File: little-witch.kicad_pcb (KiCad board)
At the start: 4 copper layers, 65 x 30 mm, 58 parts, among them J1 GCT-USB4105, J2 TMJG0803HENL, J3 Conn_ARM_SWD_TagConnect_TC203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, J4 GCT-USB4105, J5 Conn_02x20_Odd_Even, J6 BOOT0_SEL, SW1 SW_Push, U1 CH32V307RCT6, U2 MXL86110C-AQB-R, Y1 SIT8008BI-73-33N-25.000000

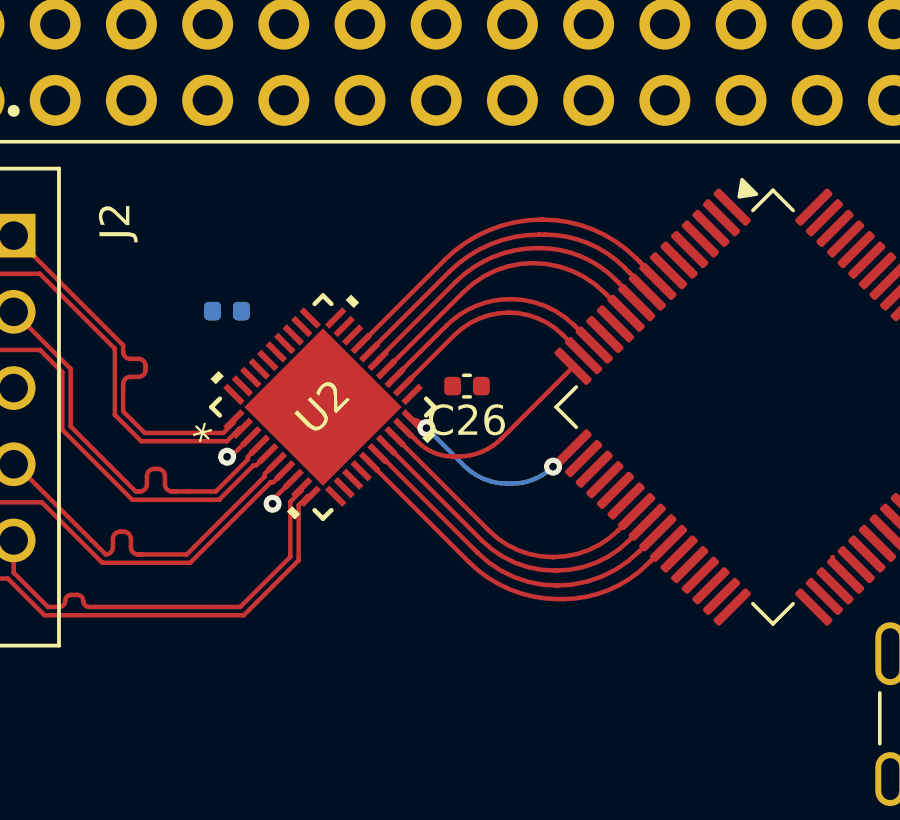
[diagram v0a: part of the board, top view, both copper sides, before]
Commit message: MDI RX/TX length matched
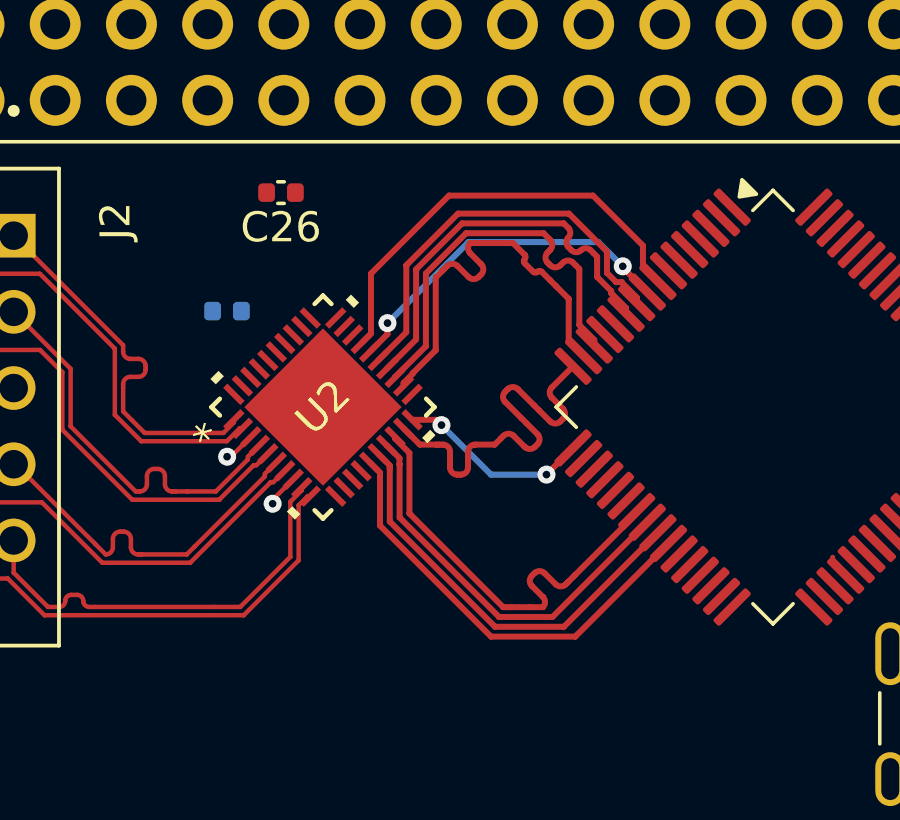
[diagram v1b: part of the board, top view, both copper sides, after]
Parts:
- moved C26 8.95 mm to (128.6, 107.8)
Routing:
- net ETH_TXC: track 7.12 -> 13.6 mm
- net ETH_RXD3: track 7.36 -> 13.6 mm
- net ETH_RXD2: track 8.07 -> 13.5 mm
- net ETH_TXD0: track 10.2 -> 14.5 mm
- net ETH_RXD1: track 9.81 -> 13.6 mm
- net ETH_RXD0: track 10.6 -> 13.7 mm
- net ETH_TXD1: track 10.8 -> 13.5 mm
- net ETH_RXC: track 12.0 -> 14.7 mm
- net ETH_TXD2: track 11.5 -> 14.1 mm
- net ETH_TXD3: track 12.2 -> 14.7 mm
- net ETH_RX_CTL: track 11.3 -> 11.7 mm, vias 0 -> 2

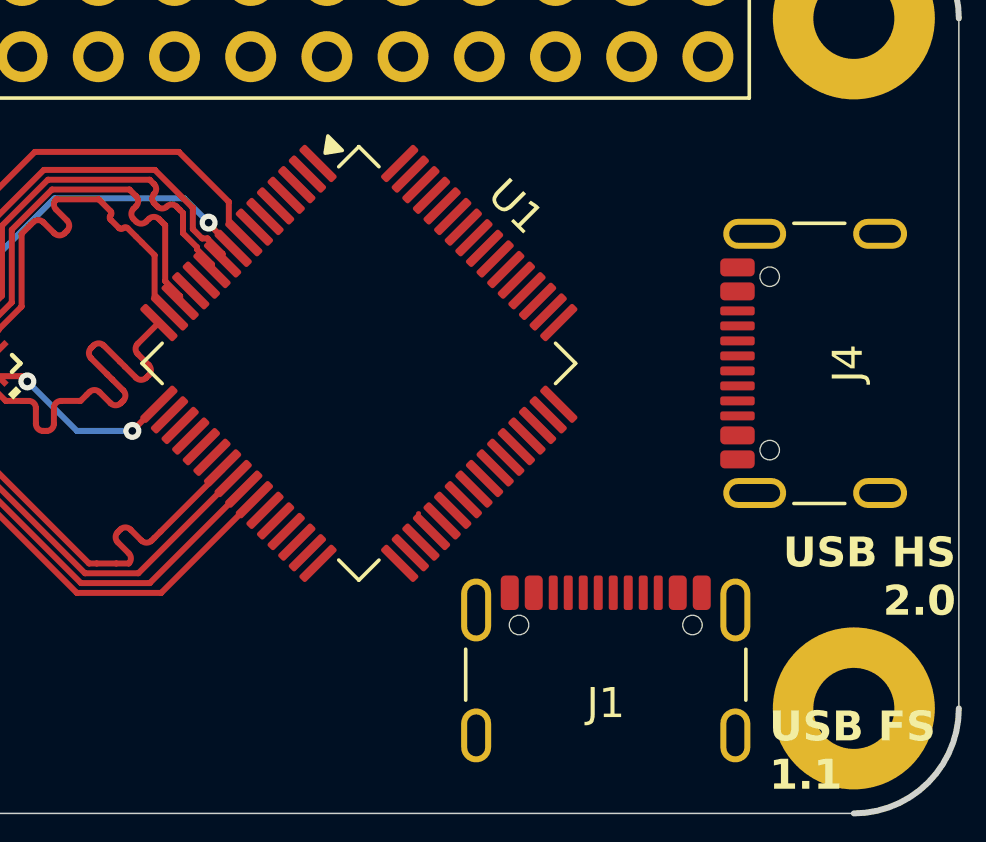
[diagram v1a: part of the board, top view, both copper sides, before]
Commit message: USB routing
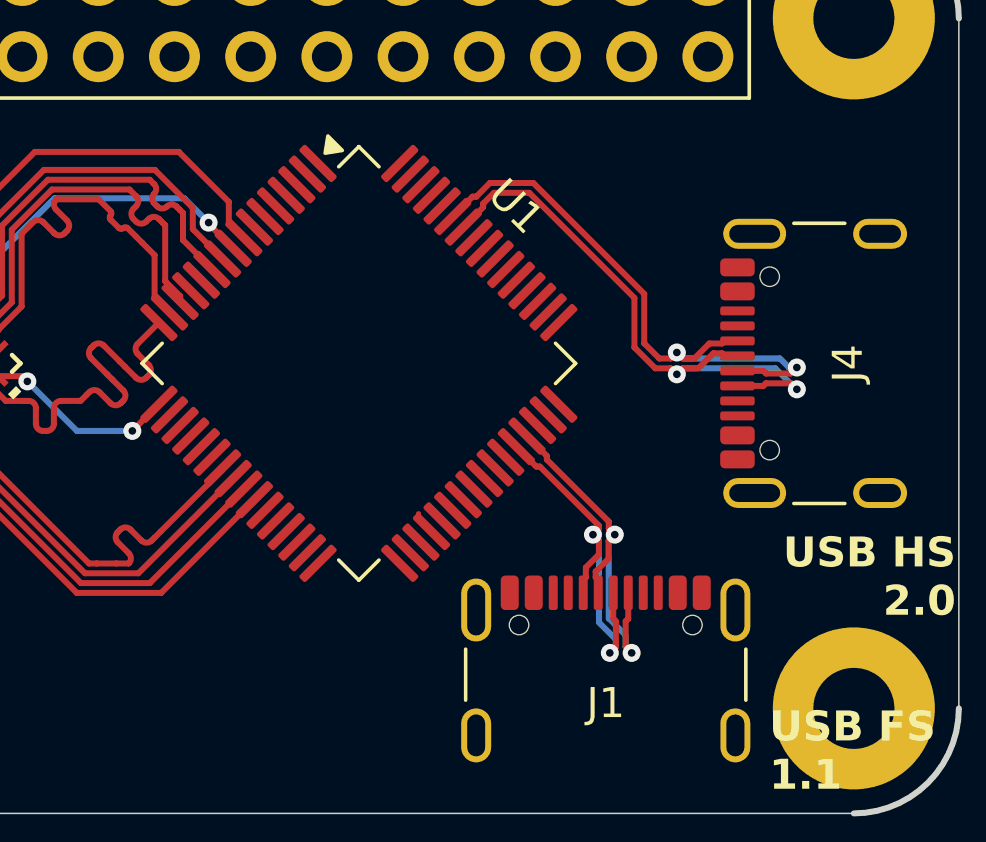
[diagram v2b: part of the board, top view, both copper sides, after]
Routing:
- net USB2_DP: track 0.00 -> 20.1 mm, vias 0 -> 2
- net USB2_DN: track 0.00 -> 20.0 mm, vias 0 -> 2
- net USB1_DP: track 0.00 -> 13.2 mm, vias 0 -> 2
- net USB1_DN: track 0.00 -> 12.9 mm, vias 0 -> 2

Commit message: MCU decoupling
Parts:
- C2, C3, C4, C5, C6: moved to B.Cu
- moved C6 57.3 mm to (152.1, 116.8), turned to 135 degrees
- moved C3 56.6 mm to (139.0, 112.2), turned to -45 degrees
- moved C2 48.9 mm to (143.2, 108.0), turned to -45 degrees
- moved C4 47.1 mm to (138.7, 117.5), turned to 45 degrees
- moved C5 20.6 mm to (143.2, 122.0), turned to 45 degrees
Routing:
- net GND: track 0.00 -> 16.8 mm, vias 0 -> 10
- net +3V3: track 0.00 -> 5.52 mm, vias 0 -> 5

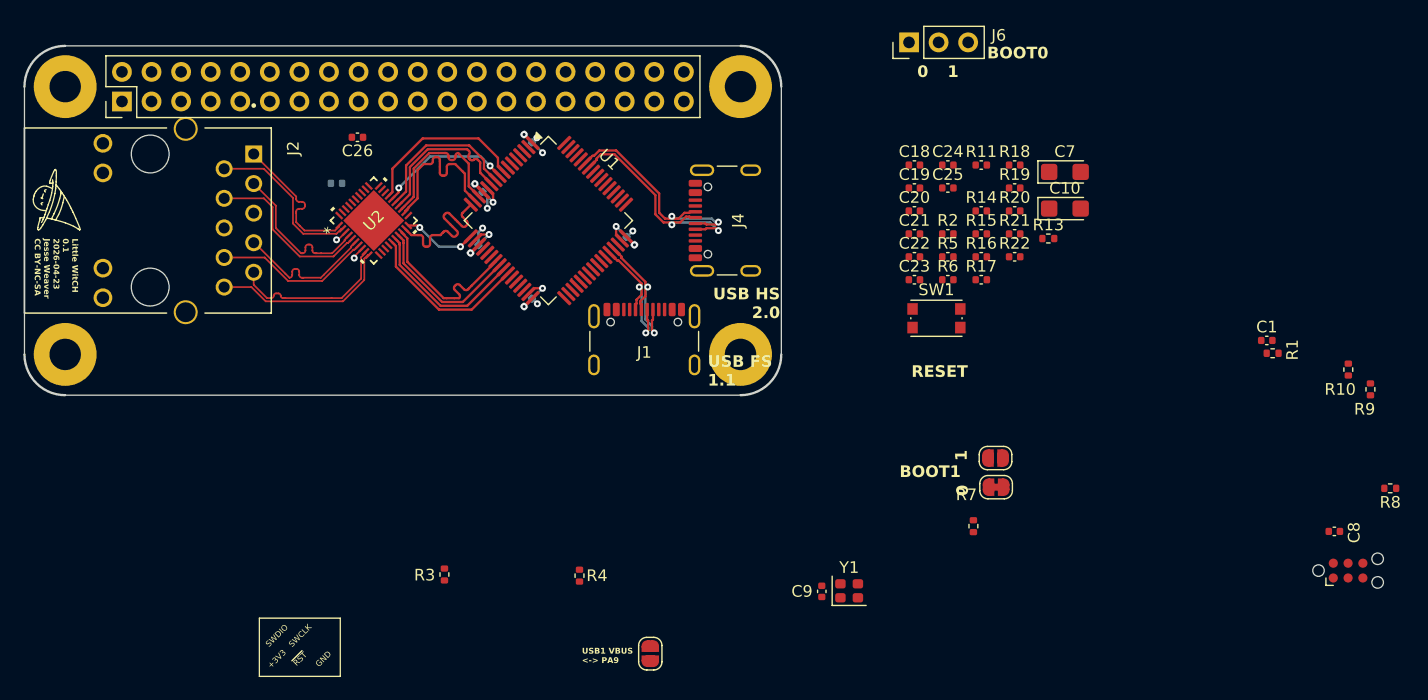
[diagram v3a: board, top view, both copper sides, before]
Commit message: Start on PHY decoupling
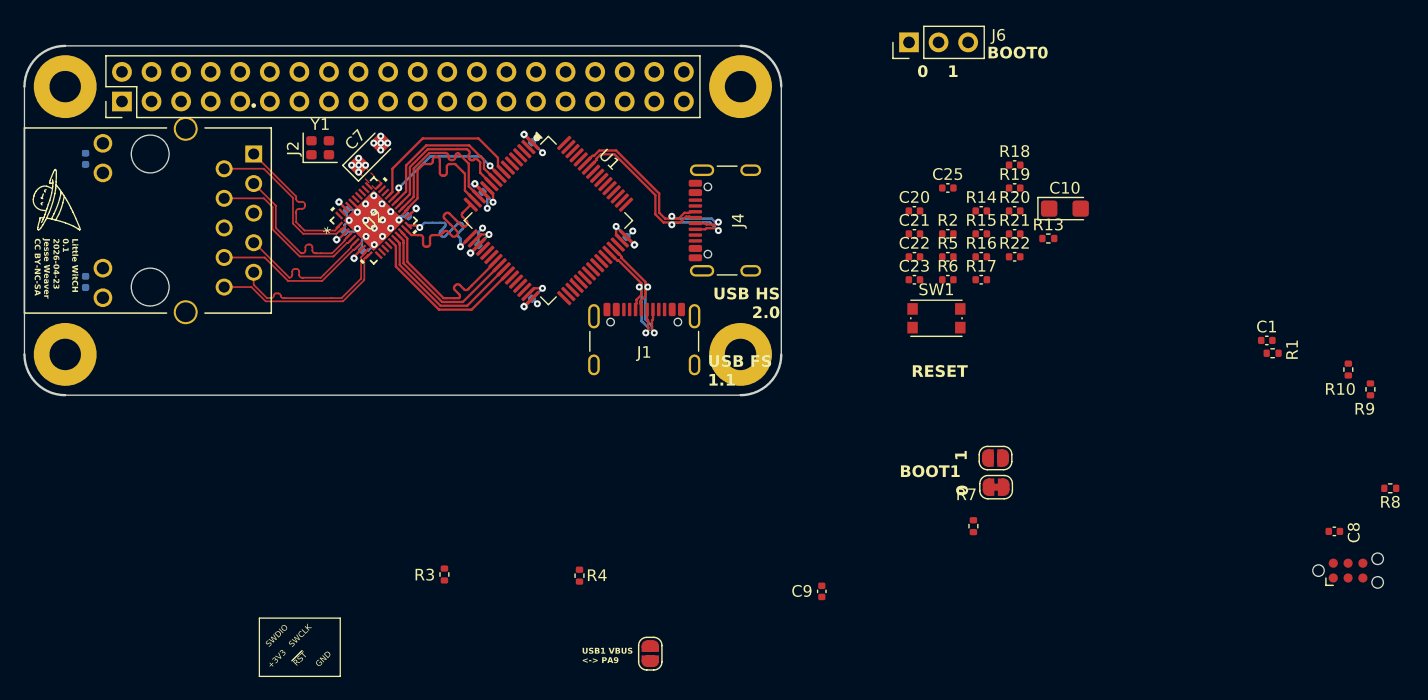
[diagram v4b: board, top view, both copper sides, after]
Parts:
- C18, C19, C24, C26, R11: moved to B.Cu
- moved R11 76.9 mm to (105.2, 109.7), turned to 90 degrees
- moved C7 59.7 mm to (129.7, 109.3), turned to 45 degrees
- moved Y1 59.3 mm to (125.4, 108.8)
- moved C18 49.7 mm to (127.2, 116.3), turned to 45 degrees
- moved C19 48.1 mm to (128.7, 117.9), turned to 45 degrees
- moved C24 46.2 mm to (133.3, 114.3), turned to -135 degrees
- moved R12 23.2 mm to (105.2, 120.3), turned to 90 degrees
- moved C26 6.03 mm to (127.3, 113.8), turned to -45 degrees
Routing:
- net GND: track 16.8 -> 27.3 mm, vias 10 -> 31
- net ETH_TX_CTL: track 6.49 -> 10.6 mm
- net VDD_ETH: track 2.17 -> 3.95 mm, vias 2 -> 9
- added copper zone on F.Cu, net VDD_ETH

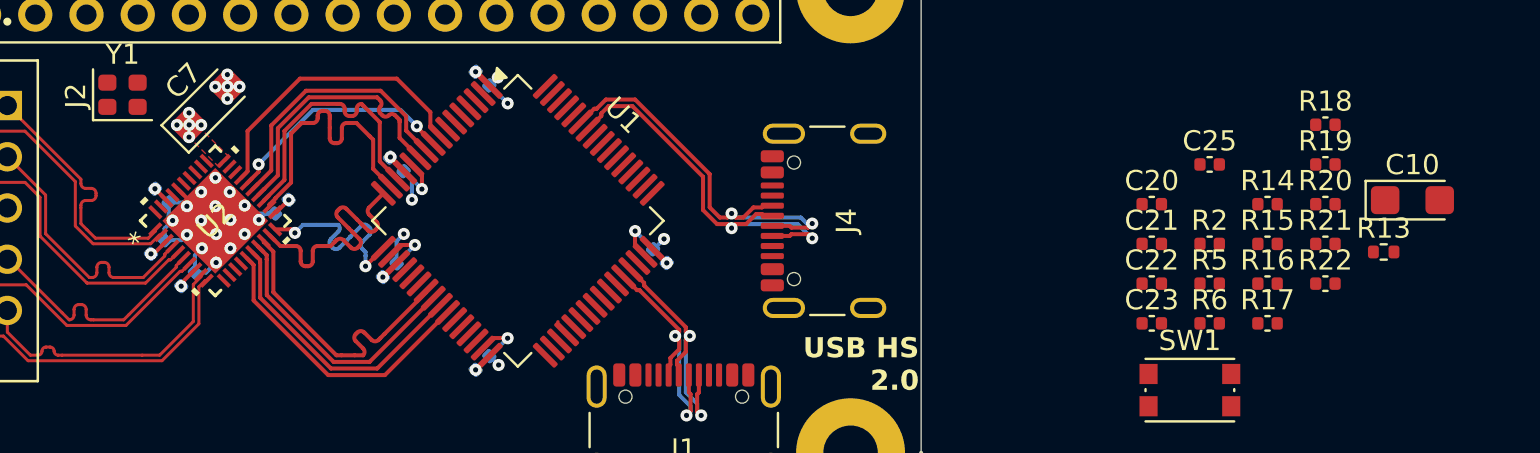
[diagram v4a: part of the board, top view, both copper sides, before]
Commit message: More PHY passives
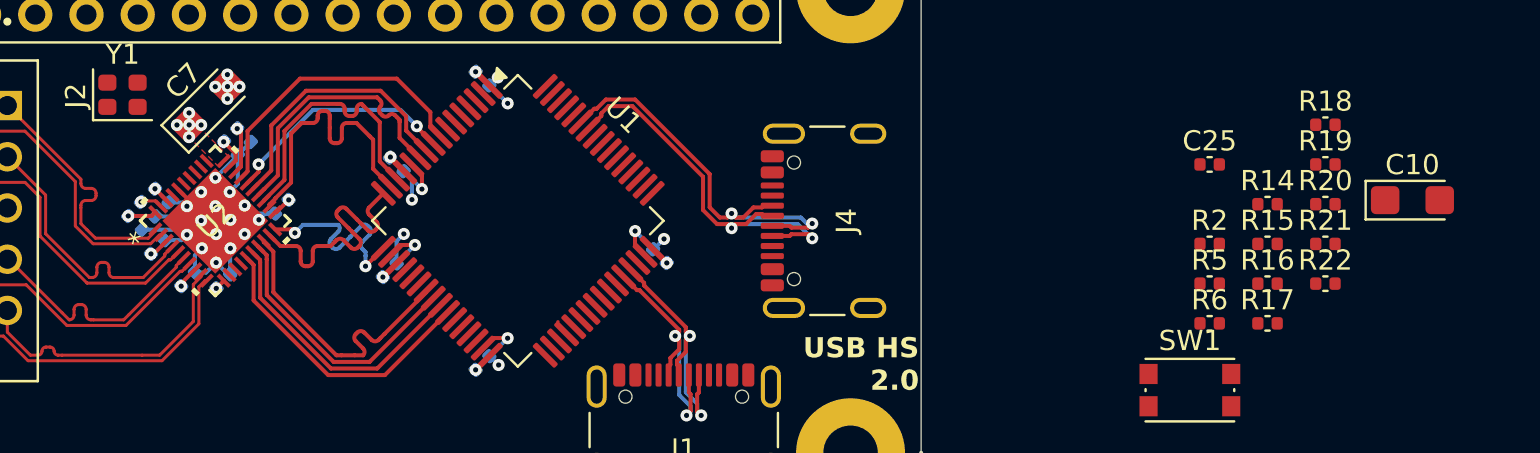
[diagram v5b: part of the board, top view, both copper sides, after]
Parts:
- C20, C21, C22, C23, R13: moved to B.Cu
- moved R13 61.3 mm to (126.7, 114.4), turned to -45 degrees
- moved C23 50.7 mm to (126.0, 115.1), turned to -45 degrees
- moved C20 46.2 mm to (130.4, 118.0), turned to 45 degrees
- moved C22 46.2 mm to (130.8, 111.4), turned to -45 degrees
- moved C21 45.3 mm to (131.4, 110.8), turned to -45 degrees
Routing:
- net GND: track 27.3 -> 36.1 mm, vias 31 -> 30
- net +3V3: track 5.52 -> 11.5 mm, vias 5 -> 9
- net Net-(U2-RCAL): track 0.00 -> 1.13 mm, vias 0 -> 1

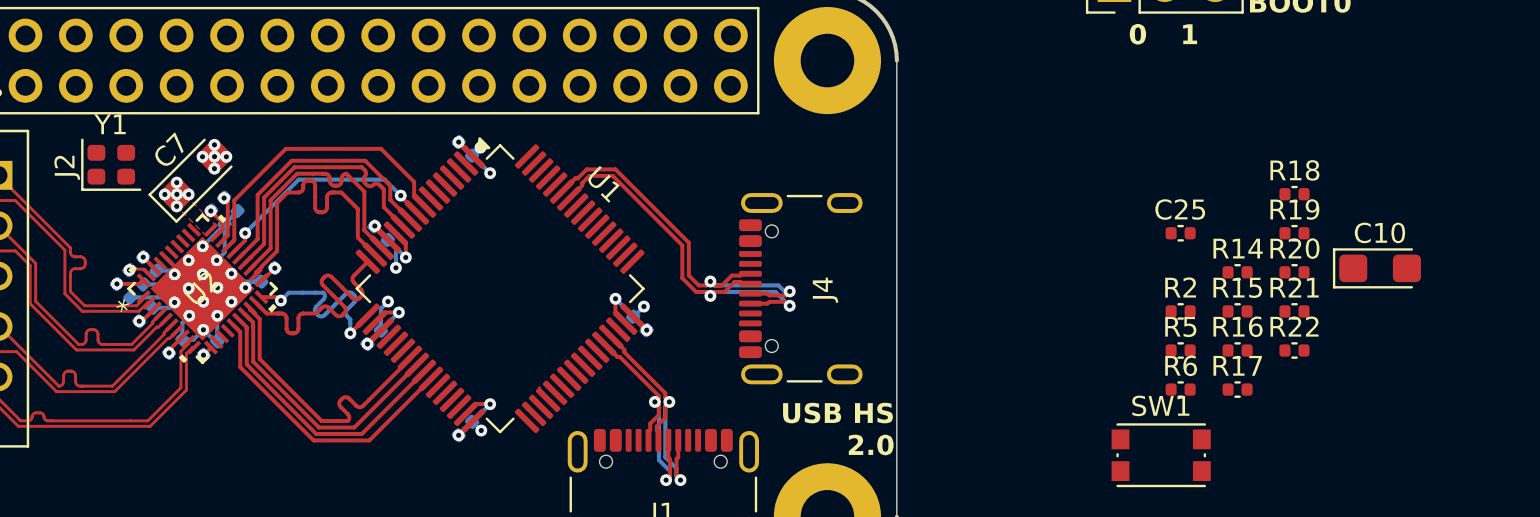
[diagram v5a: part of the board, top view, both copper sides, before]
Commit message: More PHY passives
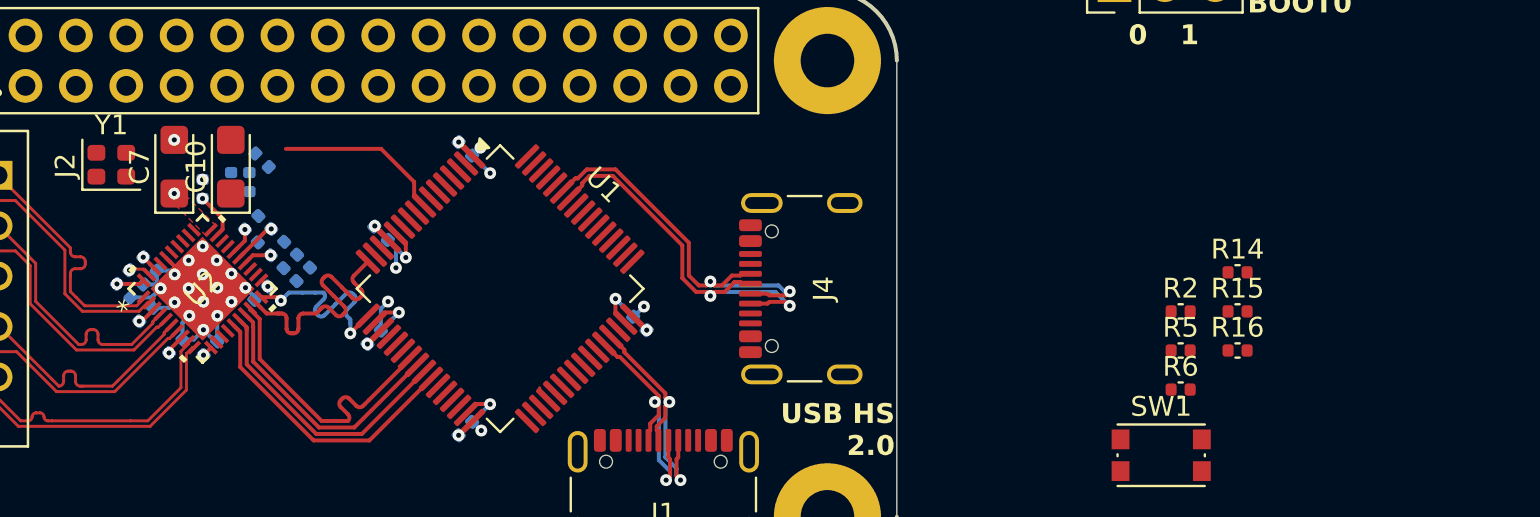
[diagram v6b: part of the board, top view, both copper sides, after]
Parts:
- C25, R17, R18, R19, R20, R21, R22: moved to B.Cu
- moved C10 58.2 mm to (131.4, 108.8), turned to 90 degrees
- moved R18 52.6 mm to (132.5, 111.7), turned to -135 degrees
- moved R20 52.4 mm to (133.0, 108.5), turned to -45 degrees
- moved R21 52.1 mm to (133.1, 112.3), turned to 45 degrees
- moved R19 51.3 mm to (133.8, 113.0), turned to -135 degrees
- moved R22 50.8 mm to (134.4, 113.6), turned to -135 degrees
- moved C25 49.4 mm to (130.0, 110.0), turned to 90 degrees
- moved R17 47.5 mm to (135.1, 114.3), turned to -135 degrees
- moved C22 1.90 mm to (131.4, 109.6), turned to 90 degrees
- moved C21 1.46 mm to (132.4, 109.6), turned to 90 degrees
- moved C7 1.17 mm to (128.6, 108.8), turned to 90 degrees
- moved C24 0.99 mm to (132.9, 115.2)
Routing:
- net ETH_RXD3: track 13.9 -> 0.00 mm
- net ETH_RXD2: track 13.5 -> 0.00 mm
- net ETH_RXD1: track 13.6 -> 1.48 mm, vias 0 -> 1
- net ETH_RXD0: track 13.6 -> 2.23 mm, vias 0 -> 1
- net ETH_RX_CTL: track 11.7 -> 1.39 mm, vias 2 -> 1
- net ETH_RXC: track 14.7 -> 8.56 mm
- net GND: track 36.1 -> 30.4 mm, vias 30 -> 28
- net +3V3: track 11.5 -> 9.88 mm, vias 9 -> 8
- net VDD_ETH: track 3.95 -> 3.47 mm, vias 9 -> 5
